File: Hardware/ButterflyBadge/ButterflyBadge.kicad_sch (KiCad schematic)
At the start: 95 parts, among them J1 USB_C_Receptacle_USB2.0, J4 Conn_02x07_Odd_Even, M1 Motor_DC, P1 TC2030-CTX, Q1 ALS-PT19, Q2 Q_NMOS_GSD, SW1 SW_Push, SW3 SW_SPDT, U1 W25Q128JVS, U2 CN3058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

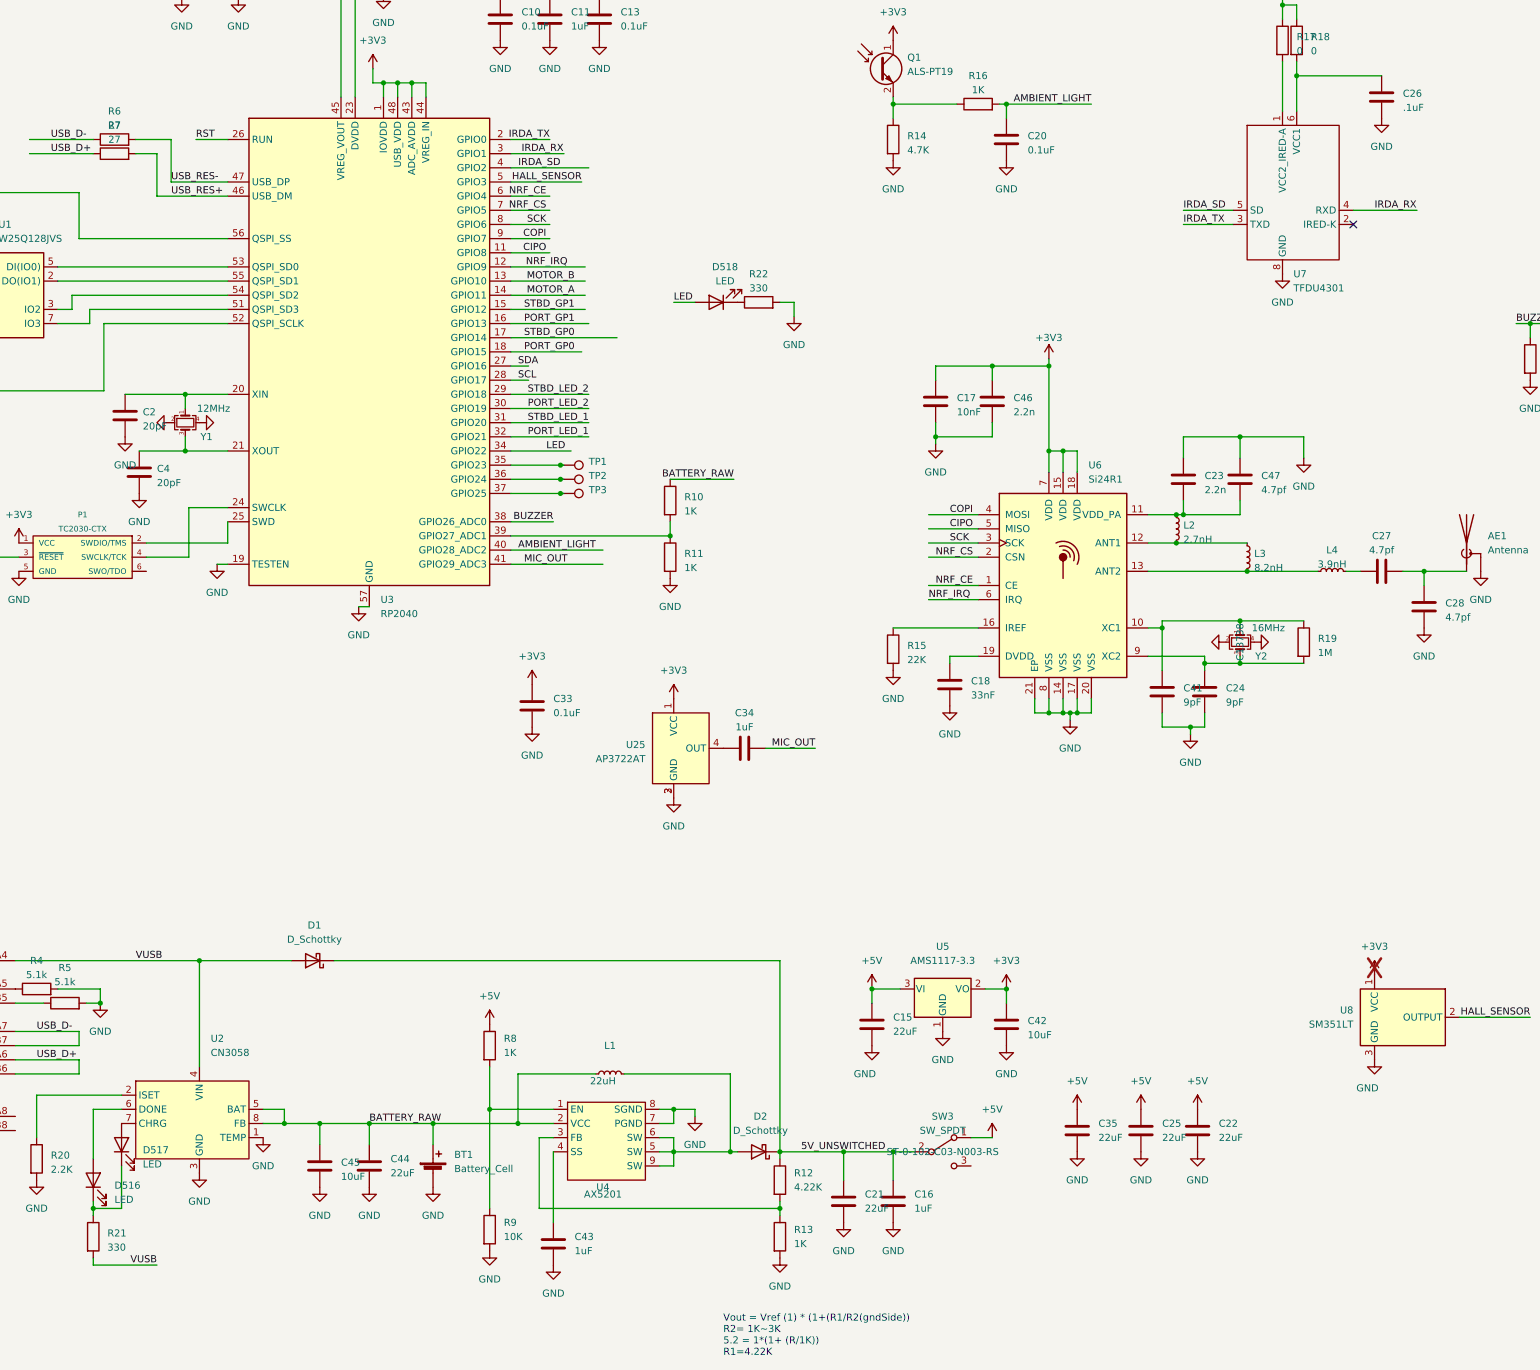
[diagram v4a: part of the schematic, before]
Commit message: Placed all the stbd wing leds
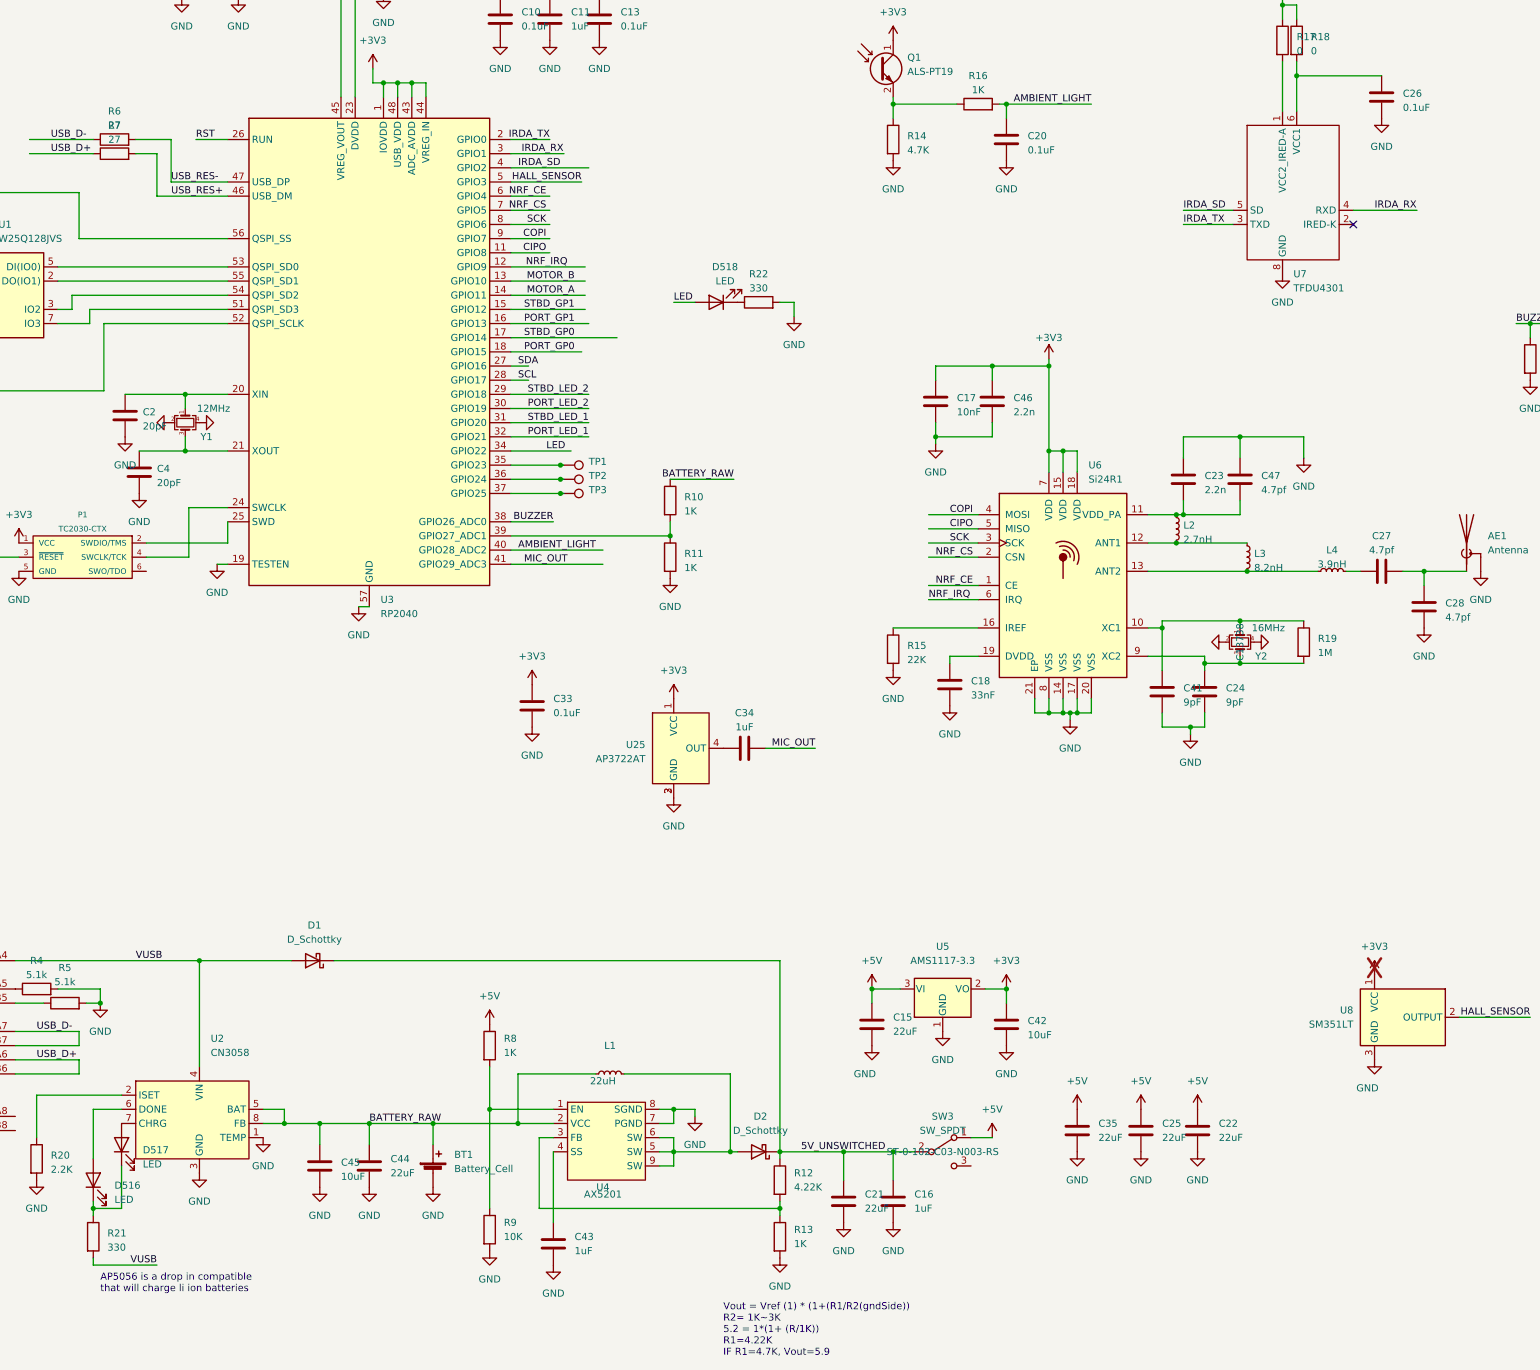
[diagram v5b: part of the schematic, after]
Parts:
- C1, C10, C13, C20, C33, C6: LCSC (none) -> C307331
- C11, C16, C29, C30, C31, C32, C34, C43, C5, C9: LCSC (none) -> C52923
- C17: LCSC (none) -> C15195
- C2, C4: LCSC (none) -> C1554
- C26: value .1uF -> 0.1uF; LCSC (none) -> C307331
- Q1: LCSC (none) -> C146233
- R1, R10, R11, R13, R16, R8: LCSC (none) -> C11702
- R12, R14: LCSC (none) -> C25900
- R17, R18, R23: LCSC (none) -> C17168
- R19: LCSC (none) -> C26083
- R2, R24, R3, R9: LCSC (none) -> C25744
- R4, R5: LCSC (none) -> C25905
- R6, R7: LCSC (none) -> C25105
- U1: LCSC (none) -> C97521
- U2: LCSC (none) -> CN3058E
- U3: LCSC (none) -> C2040
- U4: LCSC (none) -> C211668
- U5: LCSC (none) -> C6186
- Y1: LCSC (none) -> C9002
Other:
- note added: "AP5056 is a drop in compatible that will charge li ion batteries"
- note added: "Vout = Vref (1) * (1+(R1/R2(gndSide)) R2= 1K~3K 5.2 = 1*(1+ (R/1K)) R1=4.22K IF R1=4.7K, Vout=5.9"
- note removed: "Vout = Vref (1) * (1+(R1/R2(gndSide)) R2= 1K~3K 5.2 = 1*(1+ (R/1K)) R1=4.22K"
